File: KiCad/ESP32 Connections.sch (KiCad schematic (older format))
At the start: 1 part

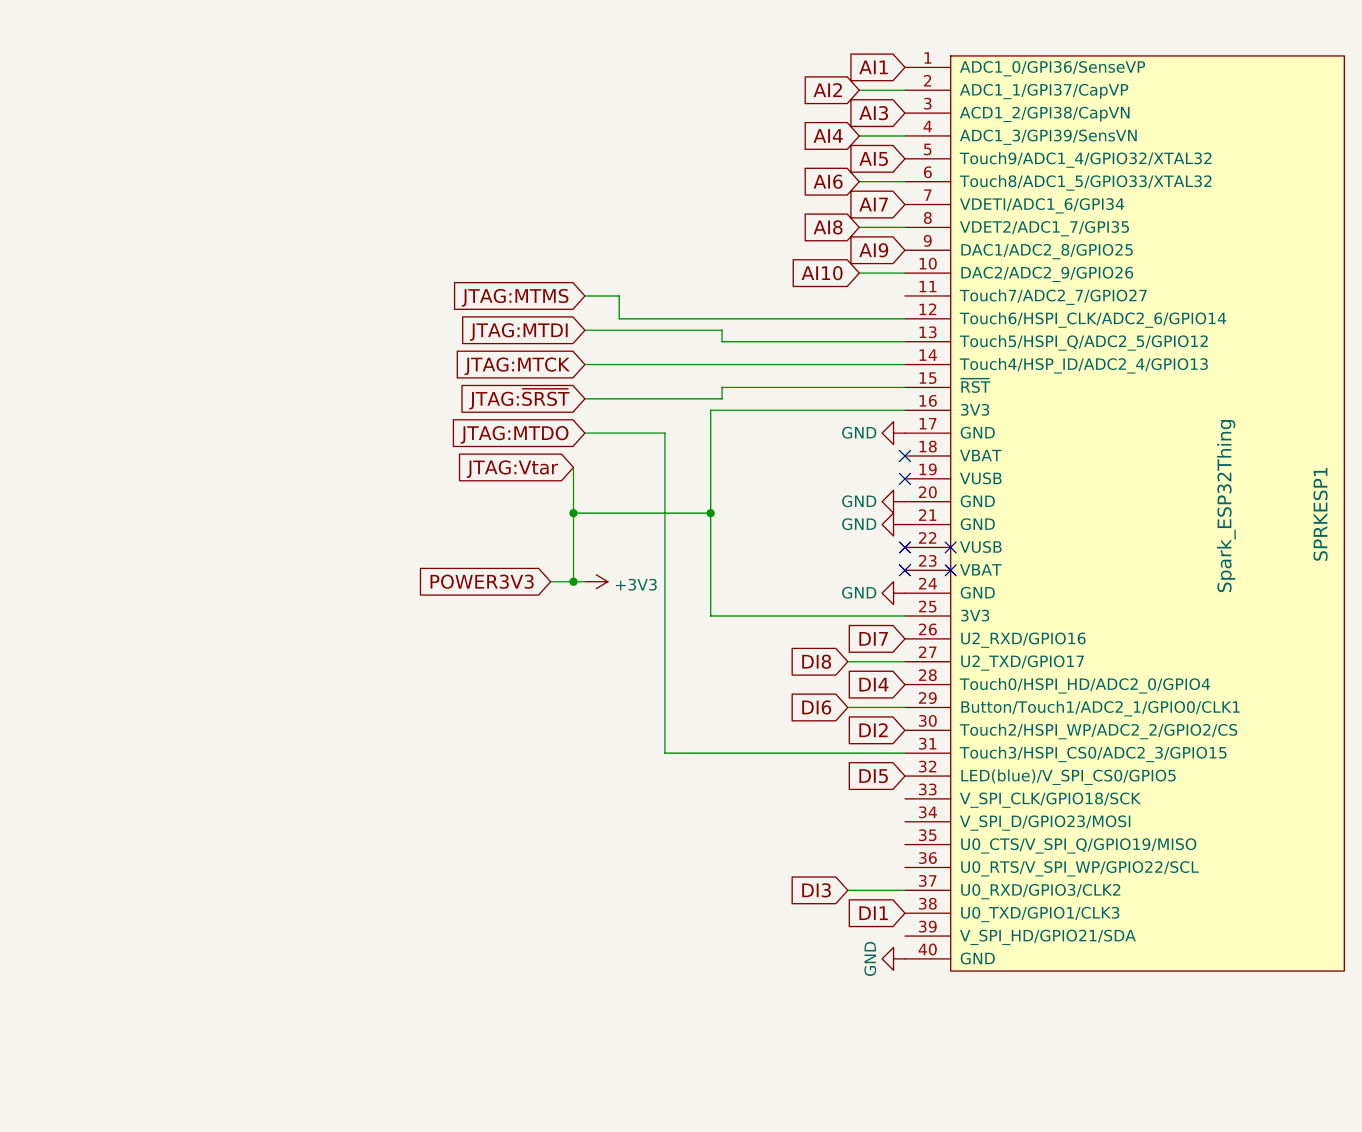
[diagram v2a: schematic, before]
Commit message: Use I2C for I/O
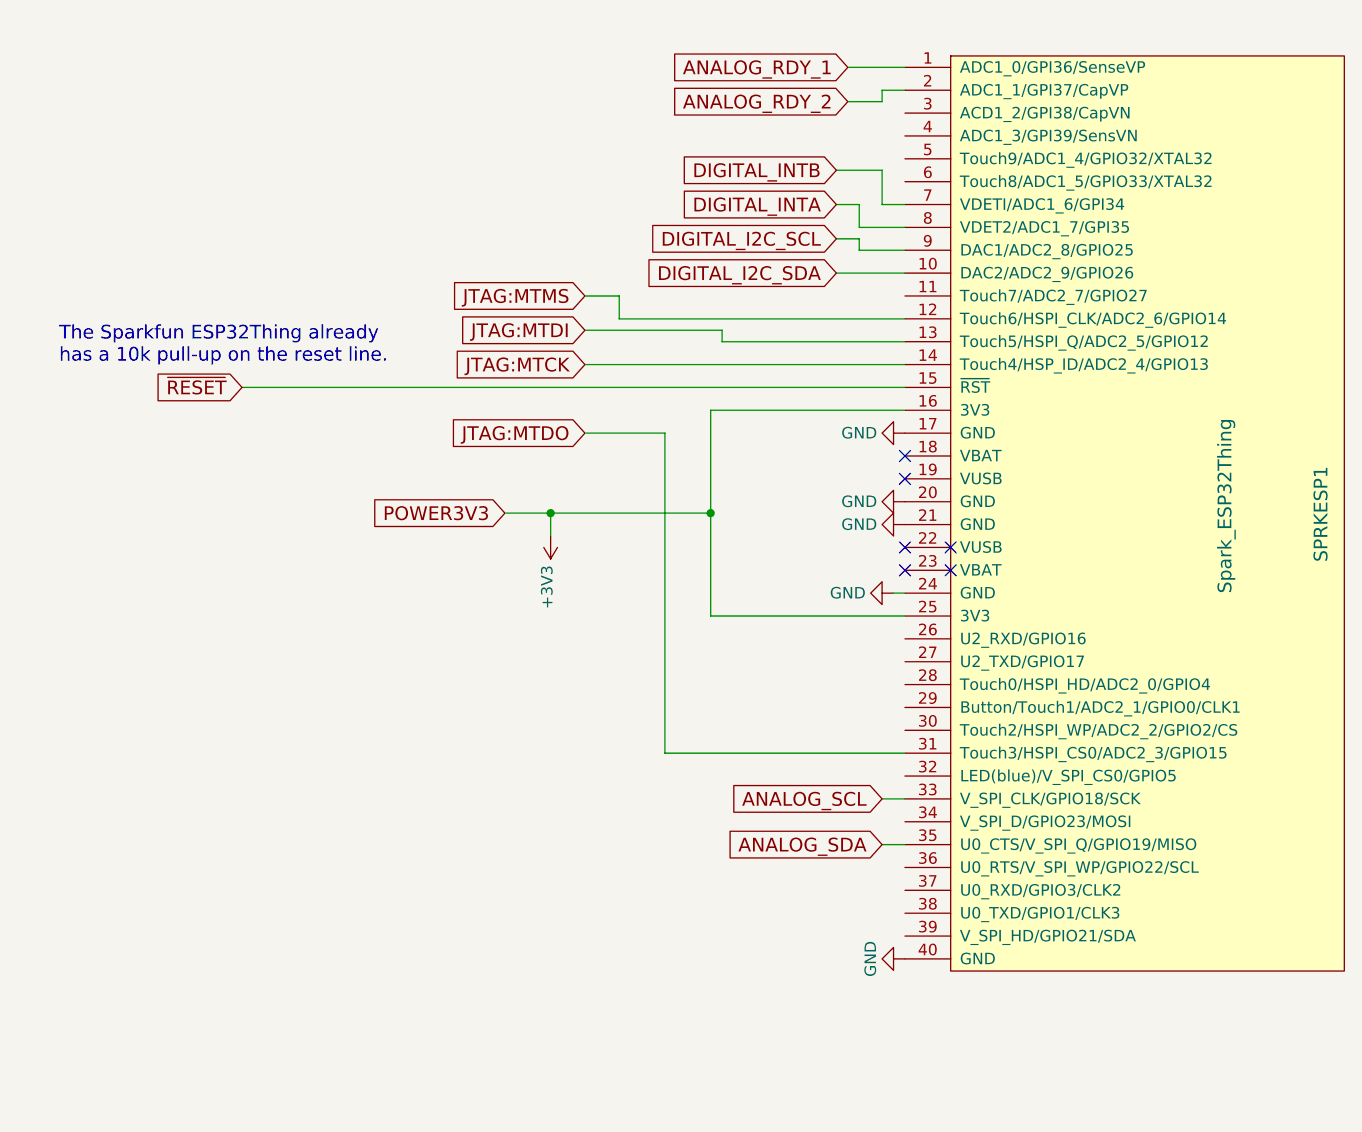
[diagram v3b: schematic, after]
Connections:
- net ANALOG_SCL: now reaches SPRKESP1.33 (V_SPI_CLK/GPIO18/SCK)
- net ANALOG_SDA: now reaches SPRKESP1.35 (U0_CTS/V_SPI_Q/GPIO19/MISO)
- net AI1 renamed ANALOG_RDY_1
- net AI10 renamed DIGITAL_I2C_SDA
- net AI2 renamed ANALOG_RDY_2
- net AI3: no longer names the net of SPRKESP1.3 (ACD1_2/GPI38/CapVN)
- net AI4: no longer names the net of SPRKESP1.4 (ADC1_3/GPI39/SensVN)
- net AI5: no longer names the net of SPRKESP1.5 (Touch9/ADC1_4/GPIO32/XTAL32)
- net AI6: no longer names the net of SPRKESP1.6 (Touch8/ADC1_5/GPIO33/XTAL32)
- net AI7 renamed DIGITAL_INTB
- net AI8 renamed DIGITAL_INTA
- net AI9 renamed DIGITAL_I2C_SCL
- net DI1: no longer names the net of SPRKESP1.38 (U0_TXD/GPIO1/CLK3)
- net DI2: no longer names the net of SPRKESP1.30 (Touch2/HSPI_WP/ADC2_2/GPIO2/CS)
- net DI3: no longer names the net of SPRKESP1.37 (U0_RXD/GPIO3/CLK2)
- net DI4: no longer names the net of SPRKESP1.28 (Touch0/HSPI_HD/ADC2_0/GPIO4)
- net DI5: no longer names the net of SPRKESP1.32 (LED(blue)/V_SPI_CS0/GPIO5)
- net DI6: no longer names the net of SPRKESP1.29 (Button/Touch1/ADC2_1/GPIO0/CLK1)
- net DI7: no longer names the net of SPRKESP1.26 (U2_RXD/GPIO16)
- net DI8: no longer names the net of SPRKESP1.27 (U2_TXD/GPIO17)
- net JTAG:~SRST renamed ~RESET
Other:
- note added: "The Sparkfun ESP32Thing already\nhas a 10k pull-up on the reset line."
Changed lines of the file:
@@
 LIBS:ESD_Protection
 LIBS:SRR1260-330M
+LIBS:ADS1115IDGST
 LIBS:HAP-IO-Card-cache
 EELAYER 26 0
@@
 NoConn ~ 5400 4200
 $Comp
-L GND #PWR018
+L GND #PWR042
 U 1 1 5918208C
 P 5200 5900
-AR Path="/59181FE5/5918208C" Ref="#PWR018"  Part="1"
-AR Path="/59181FE5/59181FE5/5918208C" Ref="#PWR018"  Part="1"
-F 0 "#PWR018" H 5200 5650 50  0001 C CNN
+F 0 "#PWR042" H 5200 5650 50  0001 C CNN
 F 1 "GND" H 5200 5750 50  0000 C CNN
 F 2 "" H 5200 5900 50  0001 C CNN
@@
 NoConn ~ 5200 3800
 $Comp
-L GND #PWR019
+L GND #PWR043
 U 1 1 59182095
 P 5200 3600
-AR Path="/59181FE5/59182095" Ref="#PWR019"  Part="1"
-AR Path="/59181FE5/59181FE5/59182095" Ref="#PWR019"  Part="1"
-F 0 "#PWR019" H 5200 3350 50  0001 C CNN
+F 0 "#PWR043" H 5200 3350 50  0001 C CNN
 F 1 "GND" V 5200 3400 50  0000 C CNN
 F 2 "" H 5200 3600 50  0001 C CNN
@@
 $EndComp
 $Comp
-L GND #PWR020
+L GND #PWR044
 U 1 1 5918209B
-P 5200 4300
-AR Path="/59181FE5/5918209B" Ref="#PWR020"  Part="1"
-AR Path="/59181FE5/59181FE5/5918209B" Ref="#PWR020"  Part="1"
-F 0 "#PWR020" H 5200 4050 50  0001 C CNN
-F 1 "GND" V 5200 4100 50  0000 C CNN
-F 2 "" H 5200 4300 50  0001 C CNN
-F 3 "" H 5200 4300 50  0001 C CNN
-	1    5200 4300
+P 5150 4300
+F 0 "#PWR044" H 5150 4050 50  0001 C CNN
+F 1 "GND" V 5150 4100 50  0000 C CNN
+F 2 "" H 5150 4300 50  0001 C CNN
+F 3 "" H 5150 4300 50  0001 C CNN
+	1    5150 4300
 	0    1    1    0
 $EndComp
@@
 U 1 1 591820B8
 P 5400 3900
-AR Path="/59181FE5/591820B8" Ref="SPRKESP1"  Part="1"
-AR Path="/59181FE5/59181FE5/591820B8" Ref="SPRKESP1"  Part="1"
 F 0 "SPRKESP1" H 5454 5520 60  0000 C CNN
 F 1 "Spark_ESP32Thing" H 5418 5100 60  0000 C CNN
@@
 $EndComp
 $Comp
-L GND #PWR021
+L GND #PWR045
 U 1 1 59184108
 P 5200 3900
-AR Path="/59181FE5/59184108" Ref="#PWR021"  Part="1"
-AR Path="/59181FE5/59181FE5/59184108" Ref="#PWR023"  Part="1"
-F 0 "#PWR021" H 5200 3650 50  0001 C CNN
+F 0 "#PWR045" H 5200 3650 50  0001 C CNN
 F 1 "GND" V 5200 3700 50  0000 C CNN
 F 2 "" H 5200 3900 50  0001 C CNN
@@
 $EndComp
 $Comp
-L GND #PWR022
+L GND #PWR046
 U 1 1 59184116
 P 5200 4000
-AR Path="/59181FE5/59184116" Ref="#PWR022"  Part="1"
-AR Path="/59181FE5/59181FE5/59184116" Ref="#PWR024"  Part="1"
-F 0 "#PWR022" H 5200 3750 50  0001 C CNN
+F 0 "#PWR046" H 5200 3750 50  0001 C CNN
 F 1 "GND" V 5200 3800 50  0000 C CNN
 F 2 "" H 5200 4000 50  0001 C CNN
@@
 	0    1    1    0
 $EndComp
-Text GLabel 5200 5700 0    60   Input ~ 0
-DI1
-Text GLabel 5200 4900 0    60   Input ~ 0
-DI2
-Text GLabel 4950 5600 0    60   Input ~ 0
-DI3
-Text GLabel 5200 4700 0    60   Input ~ 0
-DI4
-Text GLabel 5200 5100 0    60   Input ~ 0
-DI5
-Text GLabel 4950 4800 0    60   Input ~ 0
-DI6
-Text GLabel 5200 4500 0    60   Input ~ 0
-DI7
-Text GLabel 4950 4600 0    60   Input ~ 0
-DI8
-Wire Wire Line
-	4950 4600 5200 4600
-Wire Wire Line
-	4950 5600 5200 5600
-Text GLabel 5200 2000 0    60   Input ~ 0
-AI1
-Text GLabel 5000 2100 0    60   Input ~ 0
-AI2
-Text GLabel 5200 2200 0    60   Input ~ 0
-AI3
-Text GLabel 5000 2300 0    60   Input ~ 0
-AI4
-Text GLabel 5000 2500 0    60   Input ~ 0
-AI6
-Text GLabel 5200 2600 0    60   Input ~ 0
-AI7
-Text GLabel 5000 2700 0    60   Input ~ 0
-AI8
-Wire Wire Line
-	5000 2100 5200 2100
-Wire Wire Line
-	5000 2300 5200 2300
-Text GLabel 5200 2800 0    60   Input ~ 0
-AI9
-Text GLabel 5000 2900 0    60   Input ~ 0
-AI10
-Text GLabel 5200 2400 0    60   Input ~ 0
-AI5
-Wire Wire Line
-	5200 2500 5000 2500
-Wire Wire Line
-	5000 2700 5200 2700
-Wire Wire Line
-	5200 2900 5000 2900
 Text GLabel 3800 3150 0    60   Input ~ 0
 JTAG:MTDI
@@
 Wire Wire Line
 	3800 3300 5200 3300
-Wire Wire Line
-	4950 4800 5200 4800
 Text GLabel 3800 3000 0    60   Input ~ 0
 JTAG:MTMS
@@
 Wire Wire Line
 	4150 3600 3800 3600
-Text GLabel 3750 3750 0    60   Input ~ 0
-JTAG:Vtar
-Text GLabel 3800 3450 0    60   Input ~ 0
-JTAG:~SRST
-Wire Wire Line
-	3800 3450 4400 3450
-Wire Wire Line
-	4400 3450 4400 3400
-Wire Wire Line
-	4400 3400 5200 3400
+Wire Wire Line
+	2300 3400 5200 3400
 Wire Wire Line
 	4150 5000 4150 3600
 NoConn ~ 5200 4200
 NoConn ~ 5200 4100
-Text GLabel 3650 4250 0    60   Input ~ 0
-POWER3V3
-$Comp
-L +3V3 #PWR?
-U 1 1 591DFCE7
-P 3800 4250
-AR Path="/59181FE5/59181FE5/591DFCE7" Ref="#PWR?"  Part="1"
-AR Path="/59181FE5/591DFCE7" Ref="#PWR023"  Part="1"
-F 0 "#PWR023" H 3800 4100 50  0001 C CNN
-F 1 "+3V3" V 3815 4378 50  0000 L CNN
-F 2 "" H 3800 4250 50  0001 C CNN
-F 3 "" H 3800 4250 50  0001 C CNN
-	1    3800 4250
-	0    1    1    0
-$EndComp
 Wire Wire Line
 	5200 3500 4350 3500
@@
 	4350 3500 4350 4400
 Wire Wire Line
-	4350 3950 3750 3950
-Connection ~ 3750 3950
+	3450 3950 4350 3950
 Wire Wire Line
 	4350 4400 5200 4400
 Connection ~ 4350 3950
-Wire Wire Line
-	3650 4250 3800 4250
-Wire Wire Line
-	3750 3750 3750 4250
-Connection ~ 3750 4250
+Text GLabel 2300 3400 0    60   Input ~ 0
+~RESET
+Text GLabel 5100 5400 0    60   Input ~ 0
+ANALOG_SDA
+Text GLabel 5100 5200 0    60   Input ~ 0
+ANALOG_SCL
+Text GLabel 4900 2600 0    60   Input ~ 0
+DIGITAL_INTA
+Text GLabel 4900 2450 0    60   Input ~ 0
+DIGITAL_INTB
+Text GLabel 4900 2750 0    60   Input ~ 0
+DIGITAL_I2C_SCL
+Text GLabel 4900 2900 0    60   Input ~ 0
+DIGITAL_I2C_SDA
+Wire Wire Line
+	5100 5200 5200 5200
+Wire Wire Line
+	5100 5400 5200 5400
+Wire Wire Line
+	4900 2900 5200 2900
+Wire Wire Line
+	4900 2750 5000 2750
+Wire Wire Line
+	5000 2750 5000 2800
+Wire Wire Line
+	5000 2800 5200 2800
+Wire Wire Line
+	5200 2700 5000 2700
+Wire Wire Line
+	5000 2700 5000 2600
+Wire Wire Line
+	5000 2600 4900 2600
+Wire Wire Line
+	4900 2450 5100 2450
+Wire Wire Line
+	5100 2450 5100 2600
+Wire Wire Line
+	5100 2600 5200 2600
+Wire Wire Line
+	5200 4300 5150 4300
+Text Notes 1500 3300 0    60   ~ 0
+The Sparkfun ESP32Thing already\nhas a 10k pull-up on the reset line.
+Text GLabel 4950 2000 0    60   Input ~ 0
+ANALOG_RDY_1
+Wire Wire Line
+	4950 2000 5200 2000
+Text GLabel 4950 2150 0    60   Input ~ 0
+ANALOG_RDY_2
+Wire Wire Line
+	4950 2150 5100 2150
+Wire Wire Line
+	5100 2150 5100 2100
+Wire Wire Line
+	5100 2100 5200 2100
+Text GLabel 3450 3950 0    60   Input ~ 0
+POWER3V3
+$Comp
+L +3V3 #PWR047
+U 1 1 592C50A9
+P 3650 4050
+F 0 "#PWR047" H 3650 3900 50  0001 C CNN
+F 1 "+3V3" V 3665 4178 50  0000 L CNN
+F 2 "" H 3650 4050 50  0001 C CNN
+F 3 "" H 3650 4050 50  0001 C CNN
+	1    3650 4050
+	-1   0    0    1
+$EndComp
+Wire Wire Line
+	3650 3950 3650 4050
+Connection ~ 3650 3950
 $EndSCHEMATC
